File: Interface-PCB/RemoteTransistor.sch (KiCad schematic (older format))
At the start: 13 parts, among them IC1 TBD62783A, IC2 TBD62783A, J6 CONN_05JST, J7 CONN_05JST, U3 CD74HC4067_MUX

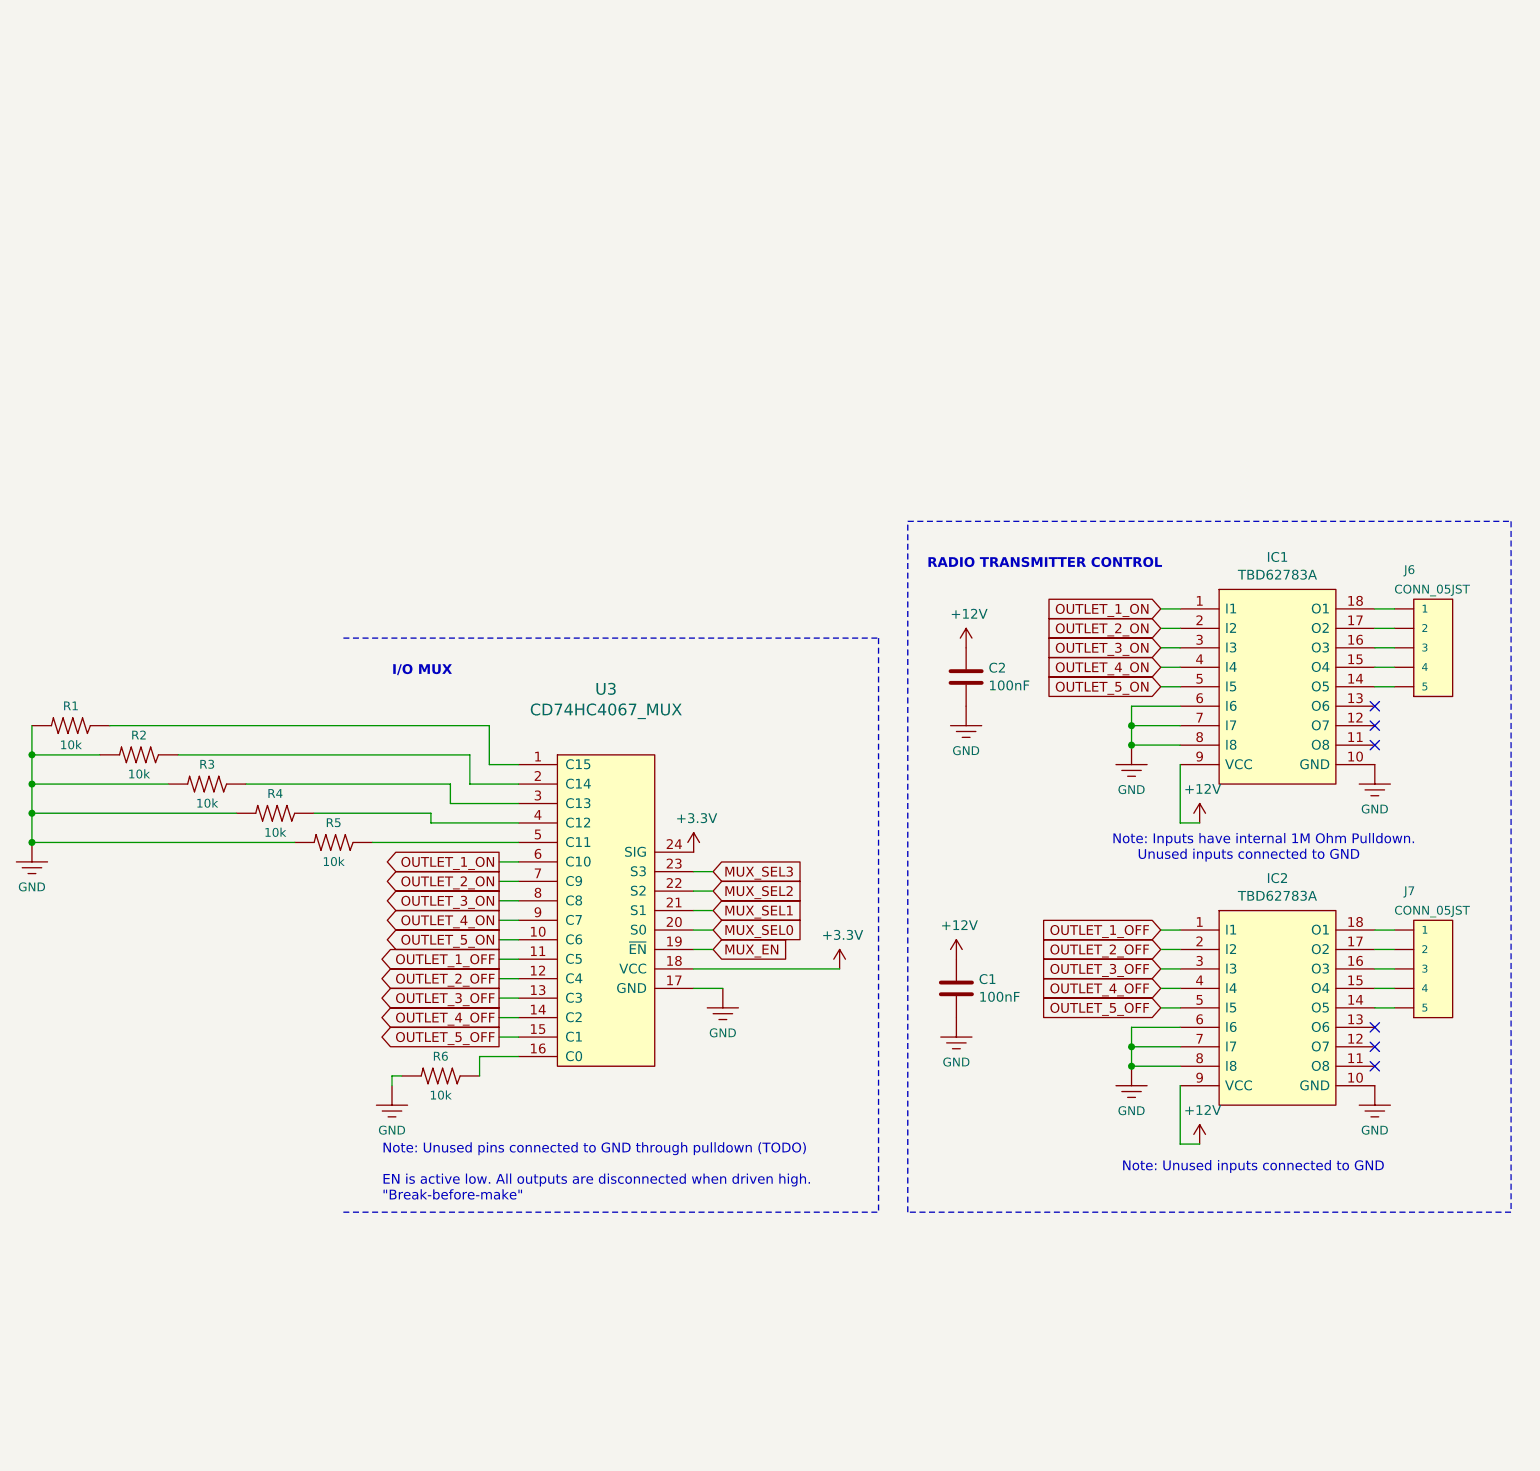
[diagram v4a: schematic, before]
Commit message: Add indicator LEDs
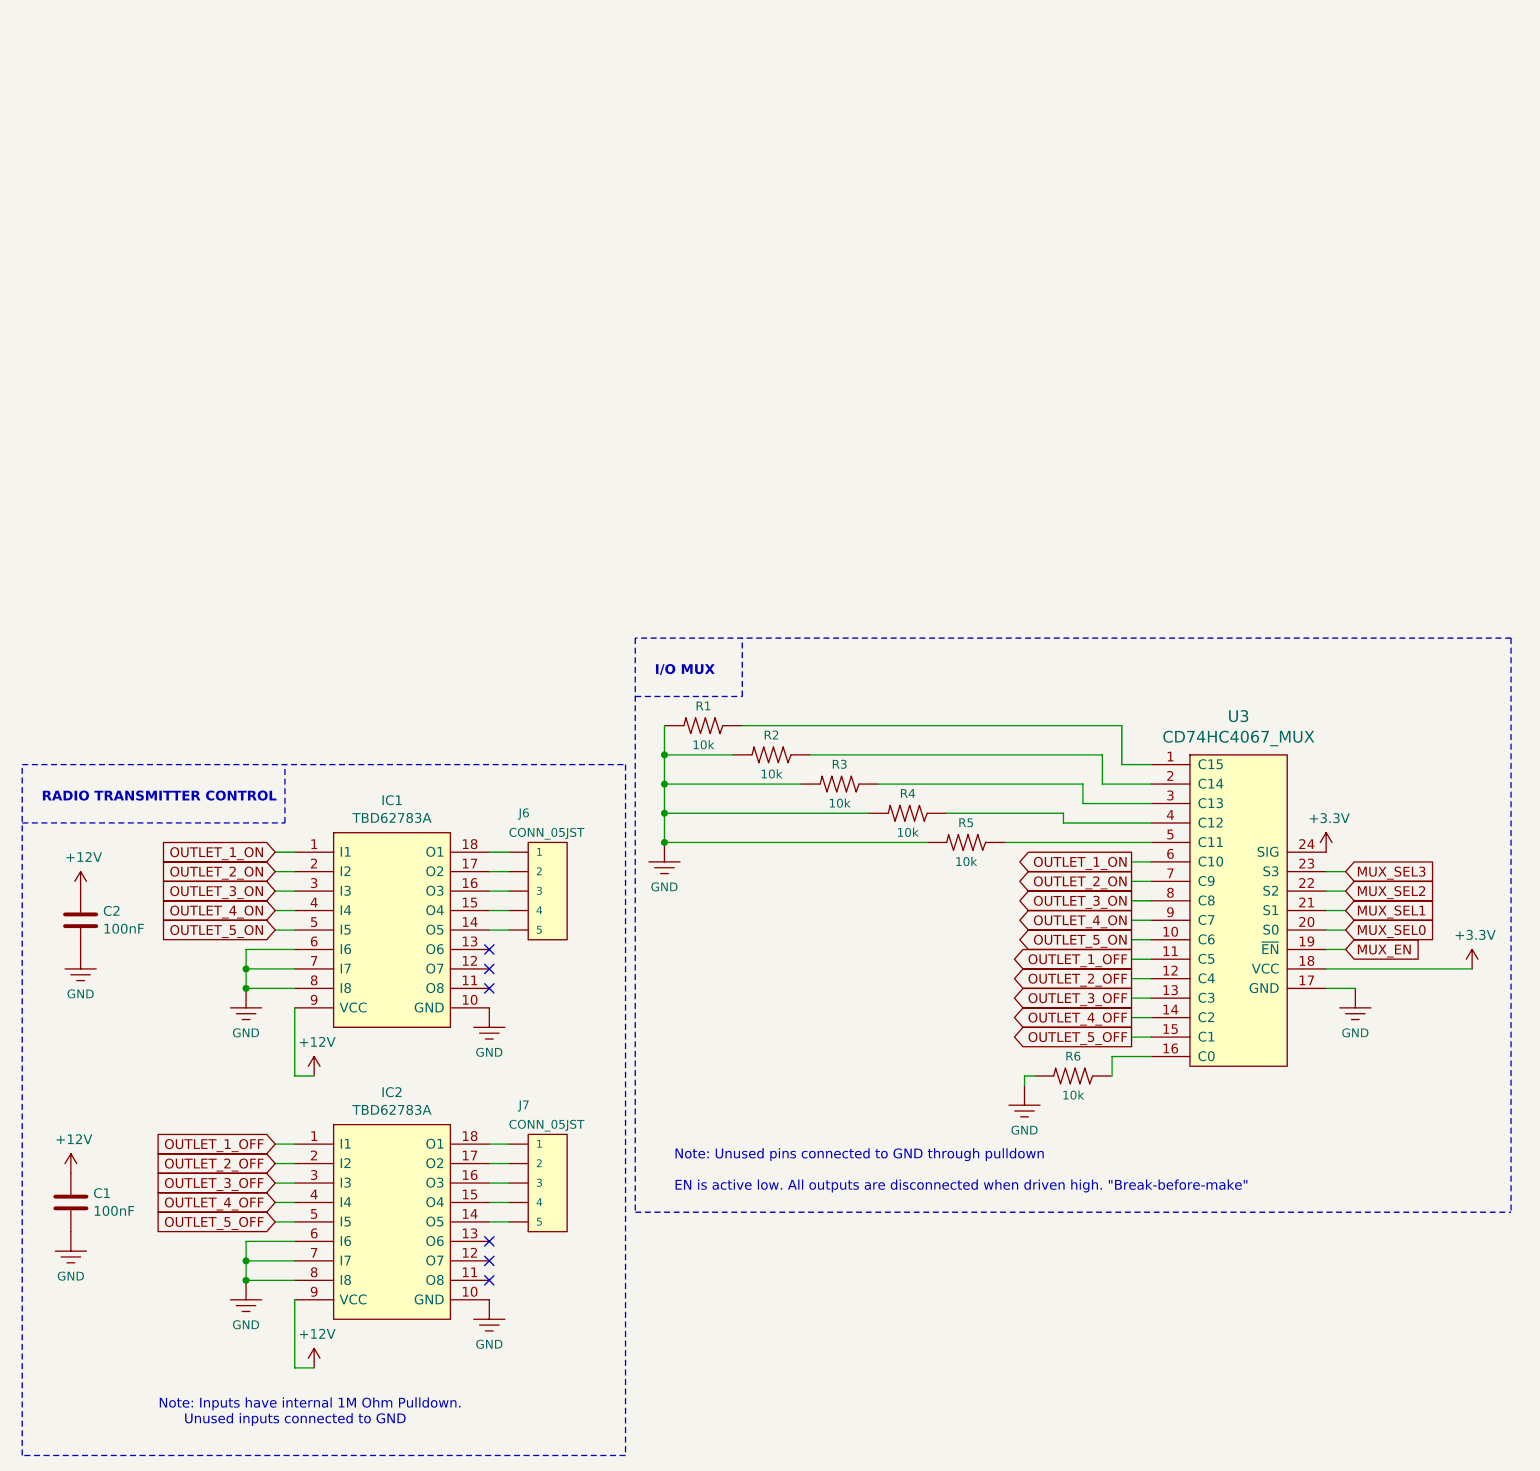
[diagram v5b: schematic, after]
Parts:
- U3: footprint Package_DIP:DIP-24_W15.24mm_LongPads -> digikey-footprints:Socket_DIP-24_15.24mm_Conn
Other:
- note added: "Note: Unused pins connected to GND through pulldown\n\nEN is active low. All outputs are disconnected when driven high. "Break-before-make""
- note removed: "Note: Unused inputs connected to GND"
- note removed: "Note: Unused pins connected to GND through pulldown (TODO)\n\nEN is active low. All outputs are disconnected when driven high.\n"Break-before-make""
- moved on the sheet: C1, C2, IC1, IC2, J6, J7, R1, R2, R3, R4, R5, R6
